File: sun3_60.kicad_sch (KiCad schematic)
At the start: 0 parts

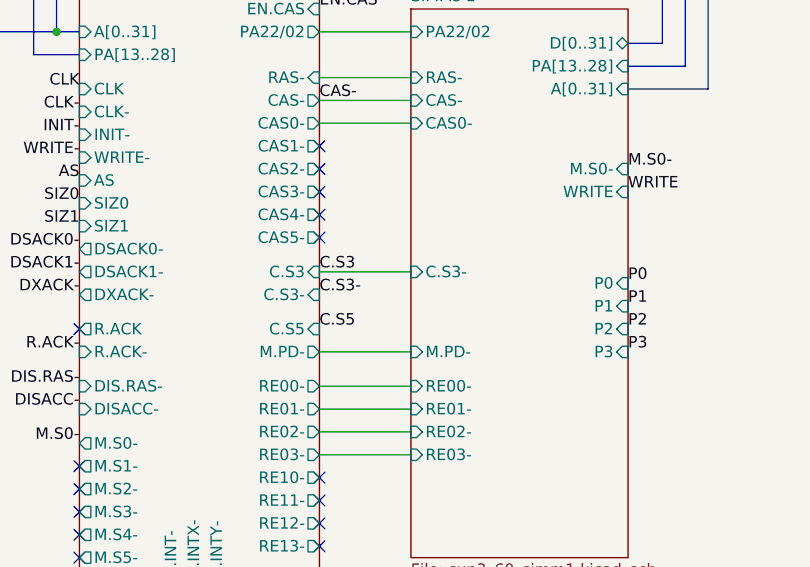
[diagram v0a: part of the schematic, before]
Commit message: Clean up before reorganizing the folders. The schematics and PCB reflect the fixes discovered during the prototype build.
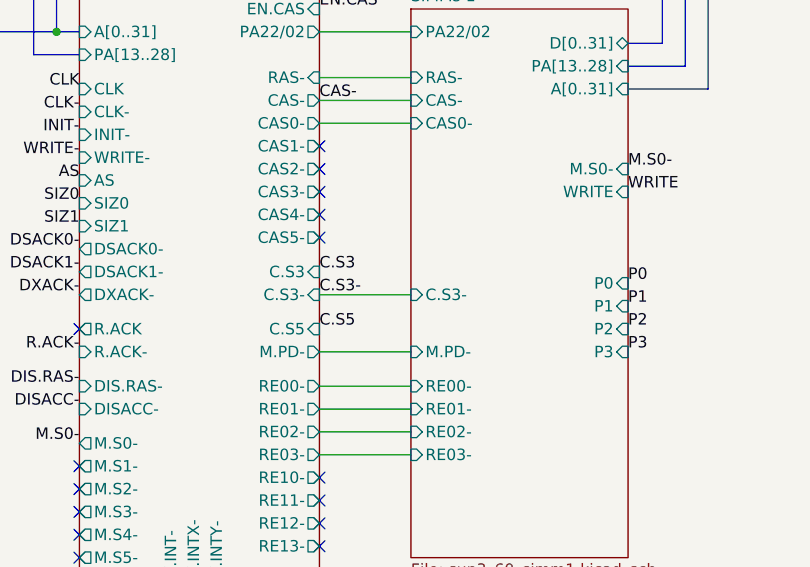
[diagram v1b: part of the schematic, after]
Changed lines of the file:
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@@
 		)
 	)
-	(wire
-		(pts
-			(xy 109.22 156.21) (xy 119.38 156.21)
-		)
-		(stroke
-			(width 0)
-			(type default)
-		)
-	)
 	(bus
 		(pts
@@
 		)
 	)
+	(wire
+		(pts
+			(xy 109.22 158.75) (xy 119.38 158.75)
+		)
+		(stroke
+			(width 0)
+			(type default)
+		)
+	)
 	(bus
 		(pts
@@
 		)
 		(pin "C.S3-" input
-			(at 119.38 156.21 180)
+			(at 119.38 158.75 180)
 			(effects
 				(font
